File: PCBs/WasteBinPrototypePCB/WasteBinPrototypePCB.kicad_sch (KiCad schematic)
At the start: 31 parts, among them J1 Jack-DC 12V, J2 Conn_01x10_Male, J3 Conn_01x06_Male, J4 SM04B-SRSS-TB(LF)(SN), Q1 MMBT3904, Q2 IRL540NSTRLPBF, U1 PC817, U2 TLV1117-50, U3 ESP32-C3-DEVKITC-02, U4 A1301EUA-T

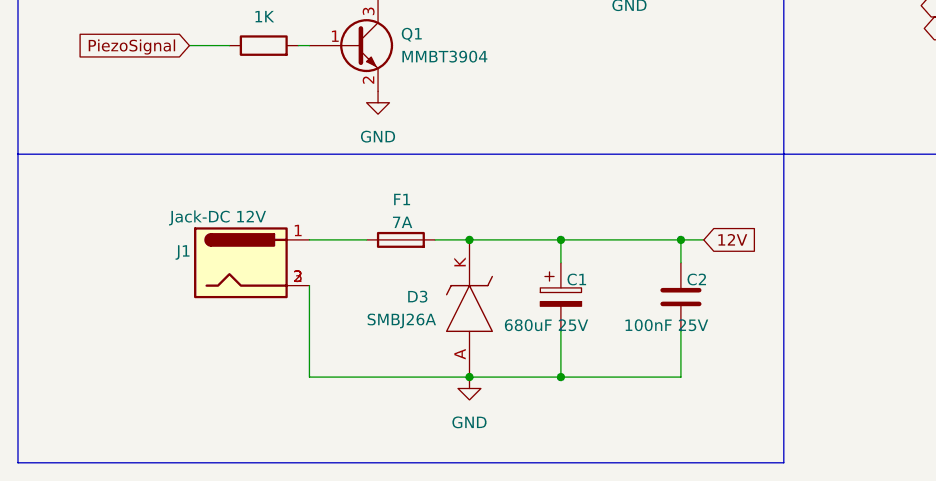
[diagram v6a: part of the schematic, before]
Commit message: added name to power input section
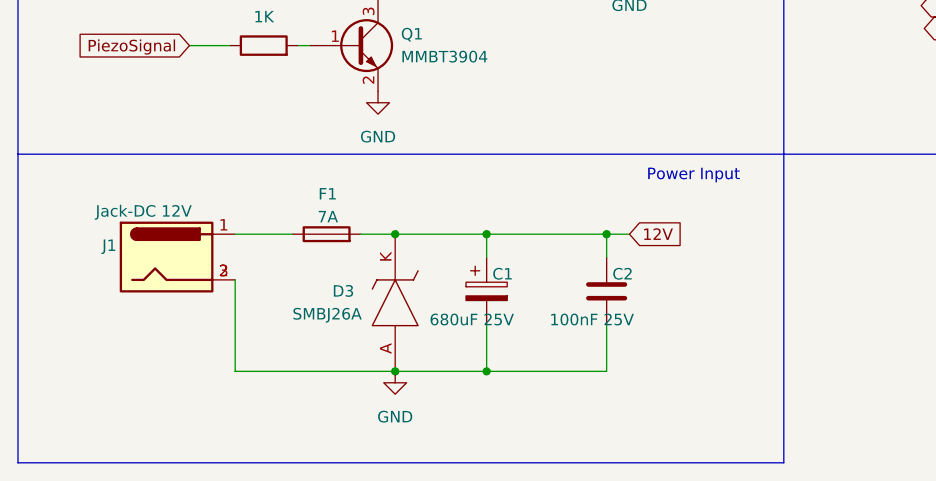
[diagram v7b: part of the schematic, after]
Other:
- note added: "Power Input"
- moved on the sheet: C1, C2, D3, F1, J1

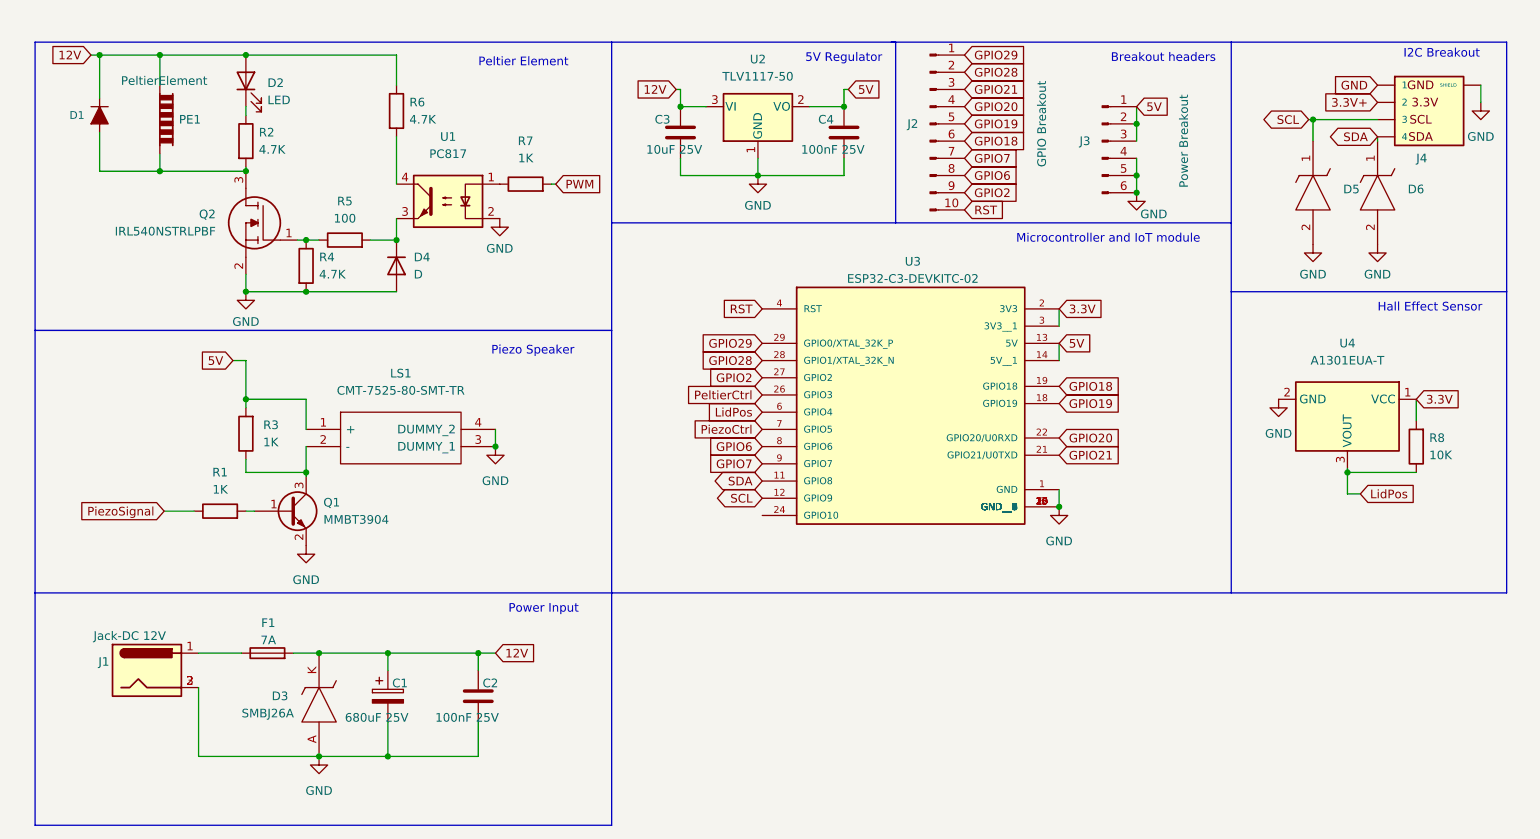
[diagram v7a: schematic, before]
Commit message: improved layout of schematic
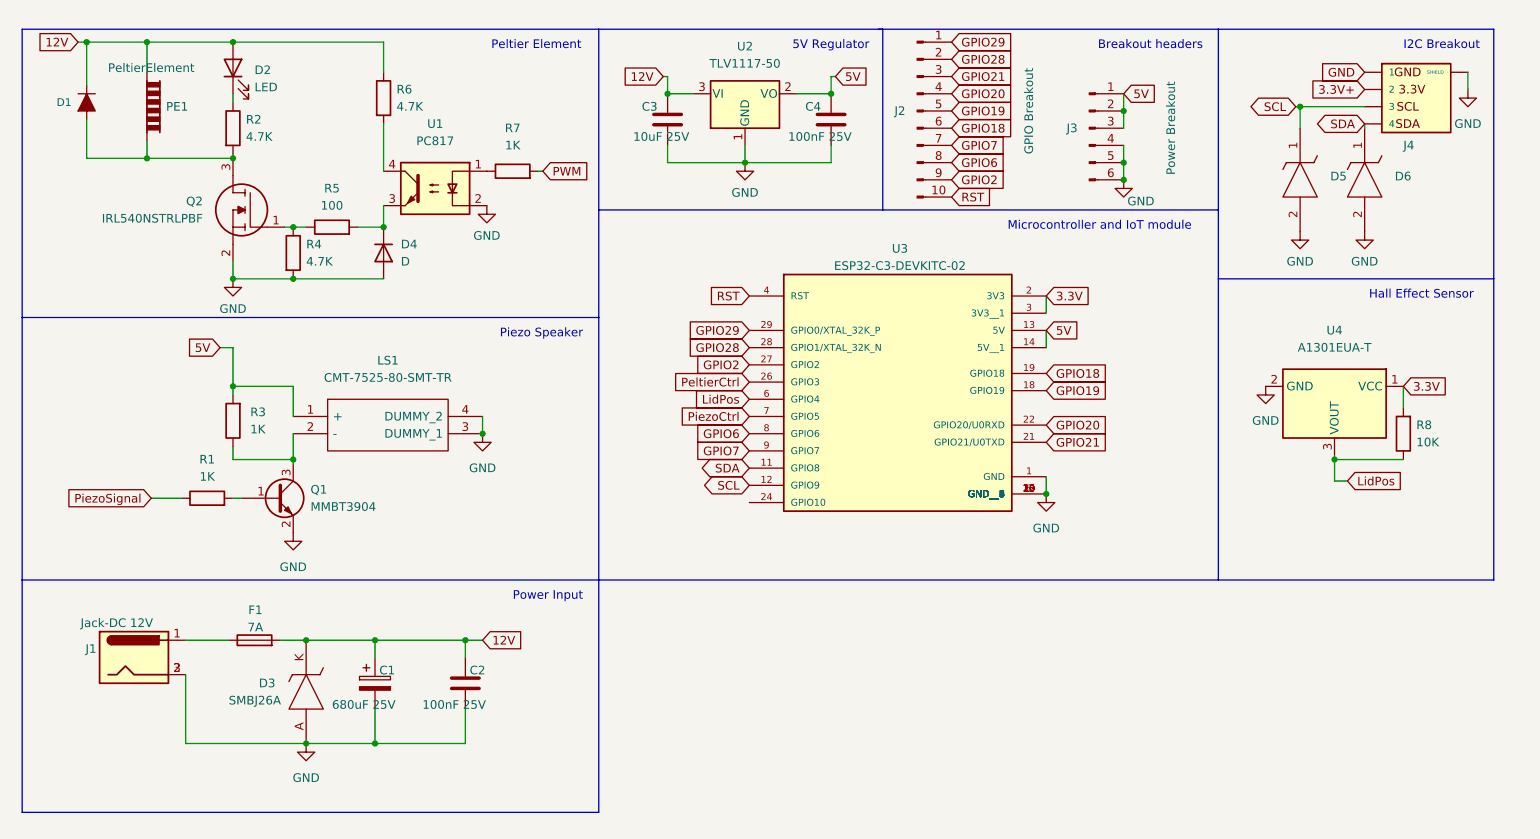
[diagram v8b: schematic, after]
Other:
- moved on the sheet: C1, C2, C3, C4, D1, D2, D3, D4, D5, D6, F1, J1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
